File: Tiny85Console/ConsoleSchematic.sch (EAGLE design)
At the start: 6 parts, among them J1 POWER_JACKSLT, U1 JOYSTICKPTH

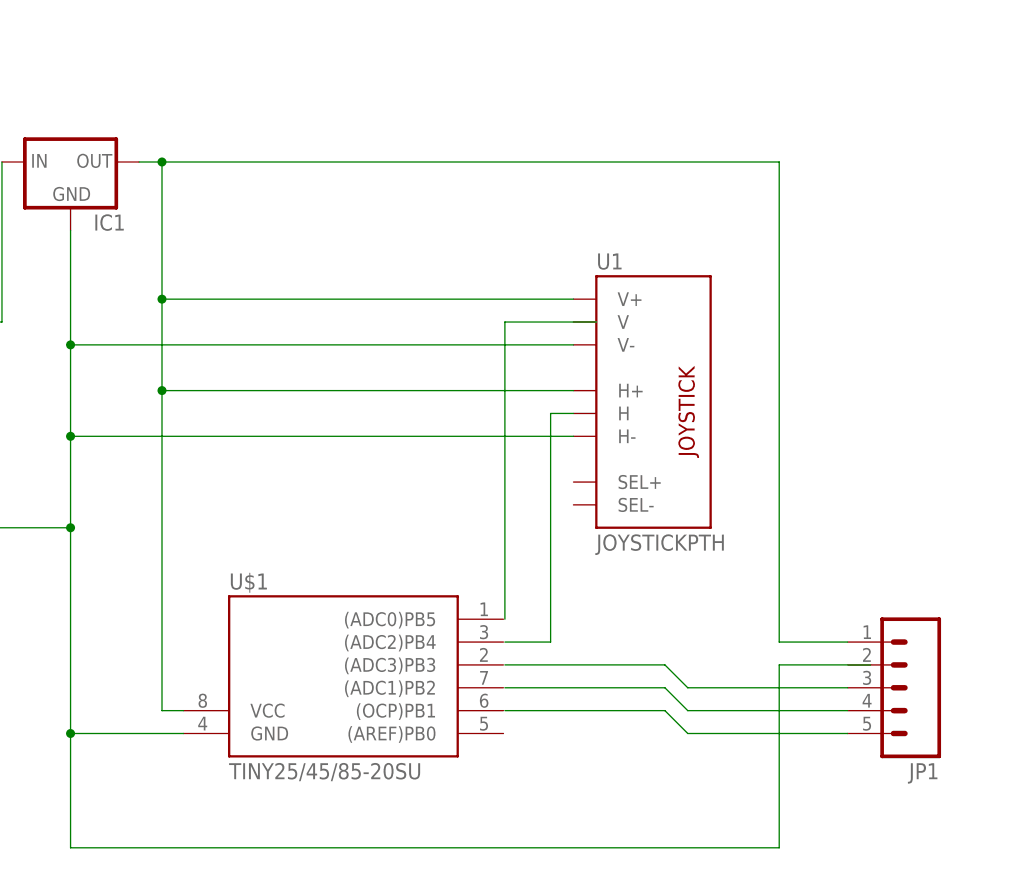
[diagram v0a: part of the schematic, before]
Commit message: Added Autorouted Design for Console.
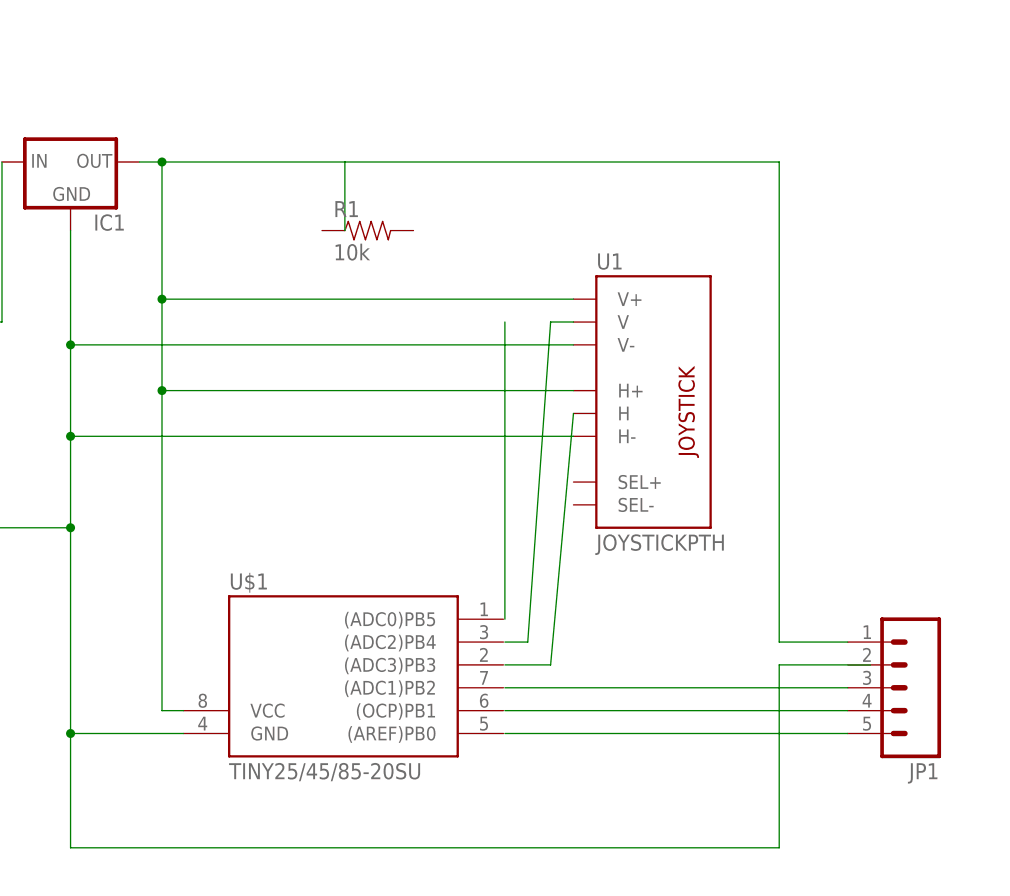
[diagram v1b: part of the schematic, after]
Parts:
- added R1: 10k, SparkFun-Resistors:10KOHM-1/4W-1%(PTH)HORIZ
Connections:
- new net N$4: U1.V
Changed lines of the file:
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@@
 <setting verticaltext="up"/>
 </settings>
-<grid distance="0.1" unitdist="inch" unit="inch" style="lines" multiple="1" display="no" altdistance="0.5" altunitdist="inch" altunit="inch"/>
+<grid distance="0.1" unitdist="inch" unit="inch" style="lines" multiple="1" display="no" altdistance="0.01" altunitdist="inch" altunit="inch"/>
 <layers>
 <layer number="1" name="Top" color="4" fill="1" visible="no" active="no"/>
@@
 <part name="U$1" library="avr-6" deviceset="TINY25/45/85" device="-20SU"/>
 <part name="JP1" library="SparkFun-Connectors" deviceset="M05" device="PTH"/>
+<part name="R1" library="SparkFun-Resistors" deviceset="10KOHM-1/4W-1%(PTH)" device="HORIZ" value="10k"/>
 </parts>
 <sheets>
@@
 <instance part="U$1" gate="G$1" x="78.58" y="76.2"/>
 <instance part="JP1" gate="G$1" x="142.24" y="76.2" rot="R180"/>
+<instance part="R1" gate="G$1" x="81.28" y="127"/>
 </instances>
 <busses>
@@
 <junction x="58.42" y="109.22"/>
 <pinref part="U$1" gate="G$1" pin="VCC"/>
-<wire x1="58.42" y1="134.62" x2="127" y2="134.62" width="0.1524" layer="91"/>
+<wire x1="58.42" y1="134.62" x2="78.74" y2="134.62" width="0.1524" layer="91"/>
+<wire x1="78.74" y1="134.62" x2="127" y2="134.62" width="0.1524" layer="91"/>
 <wire x1="127" y1="134.62" x2="127" y2="81.28" width="0.1524" layer="91"/>
 <junction x="58.42" y="134.62"/>
 <wire x1="127" y1="81.28" x2="134.62" y2="81.28" width="0.1524" layer="91"/>
+<wire x1="78.74" y1="134.62" x2="78.74" y2="127" width="0.1524" layer="91"/>
 </segment>
 </net>
@@
 <segment>
 <wire x1="96.52" y1="83.82" x2="96.52" y2="116.84" width="0.1524" layer="91"/>
-<wire x1="96.52" y1="116.84" x2="106.68" y2="116.84" width="0.1524" layer="91"/>
 </segment>
 </net>
 <net name="N$4" class="0">
 <segment>
-<wire x1="96.52" y1="81.28" x2="101.6" y2="81.28" width="0.1524" layer="91"/>
-<wire x1="101.6" y1="81.28" x2="101.6" y2="106.68" width="0.1524" layer="91"/>
+<wire x1="96.52" y1="81.28" x2="99.06" y2="81.28" width="0.1524" layer="91"/>
+<pinref part="U1" gate="G$1" pin="V"/>
+<wire x1="99.06" y1="81.28" x2="101.6" y2="116.84" width="0.1524" layer="91"/>
+<wire x1="101.6" y1="116.84" x2="104.14" y2="116.84" width="0.1524" layer="91"/>
+</segment>
+</net>
+<net name="N$5" class="0">
+<segment>
+<wire x1="96.52" y1="78.74" x2="101.6" y2="78.74" width="0.1524" layer="91"/>
 <pinref part="U1" gate="G$1" pin="H"/>
-<wire x1="101.6" y1="106.68" x2="104.14" y2="106.68" width="0.1524" layer="91"/>
-</segment>
-</net>
-<net name="N$5" class="0">
-<segment>
-<wire x1="96.52" y1="78.74" x2="114.3" y2="78.74" width="0.1524" layer="91"/>
-<wire x1="114.3" y1="78.74" x2="116.84" y2="76.2" width="0.1524" layer="91"/>
+<wire x1="101.6" y1="78.74" x2="104.14" y2="106.68" width="0.1524" layer="91"/>
+</segment>
+</net>
+<net name="N$7" class="0">
+<segment>
+<pinref part="JP1" gate="G$1" pin="4"/>
+<wire x1="96.52" y1="73.66" x2="134.62" y2="73.66" width="0.1524" layer="91"/>
+</segment>
+</net>
+<net name="N$8" class="0">
+<segment>
+<pinref part="JP1" gate="G$1" pin="5"/>
+<wire x1="96.52" y1="71.12" x2="134.62" y2="71.12" width="0.1524" layer="91"/>
+</segment>
+</net>
+<net name="N$6" class="0">
+<segment>
 <pinref part="JP1" gate="G$1" pin="3"/>
-<wire x1="116.84" y1="76.2" x2="134.62" y2="76.2" width="0.1524" layer="91"/>
-</segment>
-</net>
-<net name="N$6" class="0">
-<segment>
-<wire x1="96.52" y1="76.2" x2="114.3" y2="76.2" width="0.1524" layer="91"/>
-<wire x1="114.3" y1="76.2" x2="116.84" y2="73.66" width="0.1524" layer="91"/>
-<pinref part="JP1" gate="G$1" pin="4"/>
-<wire x1="116.84" y1="73.66" x2="134.62" y2="73.66" width="0.1524" layer="91"/>
-</segment>
-</net>
-<net name="N$7" class="0">
-<segment>
-<wire x1="96.52" y1="73.66" x2="114.3" y2="73.66" width="0.1524" layer="91"/>
-<wire x1="114.3" y1="73.66" x2="116.84" y2="71.12" width="0.1524" layer="91"/>
-<pinref part="JP1" gate="G$1" pin="5"/>
-<wire x1="116.84" y1="71.12" x2="134.62" y2="71.12" width="0.1524" layer="91"/>
-</segment>
-</net>
+<wire x1="96.52" y1="76.2" x2="134.62" y2="76.2" width="0.1524" layer="91"/>
+</segment>
+</net>
